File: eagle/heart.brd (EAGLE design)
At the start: 29.8 x 25.5 mm, 8 parts

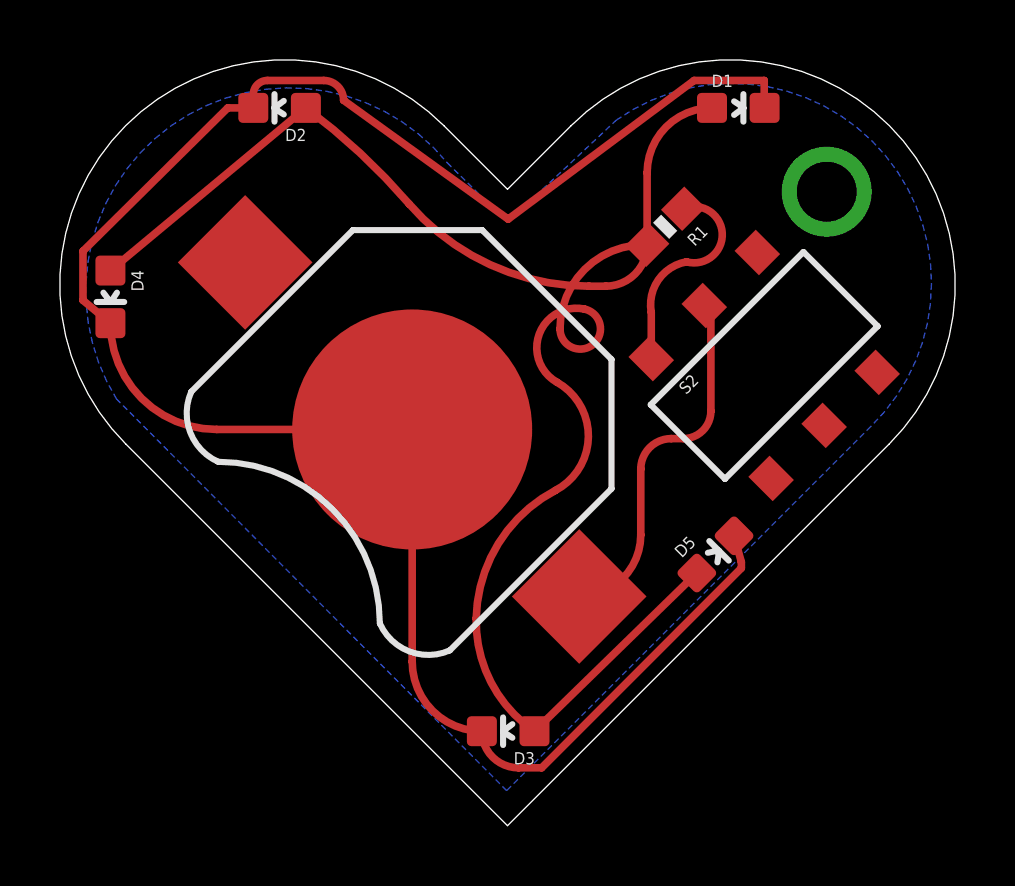
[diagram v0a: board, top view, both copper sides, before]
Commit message: move eagle files to `eagle` dir
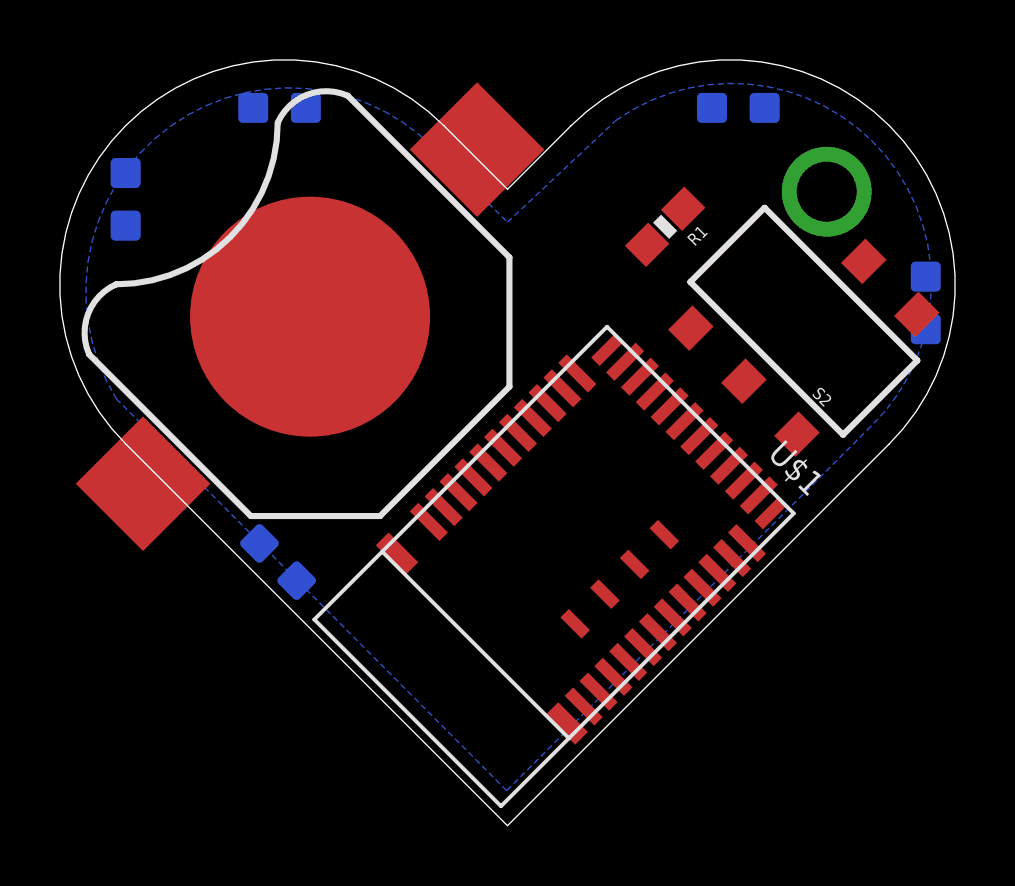
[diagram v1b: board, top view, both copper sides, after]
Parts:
- added U$1: MDBT42, MDBT42:MDBT42
- moved D3 19.9 mm to (30.7, 18.0), flipped to the bottom, turned to 0 degrees
- moved D5 14.6 mm to (9.14, 9.40), flipped to the bottom, turned to 135 degrees
- moved BAT1 5.07 mm to (10.2, 17.6), turned to 45 degrees
- moved D4 3.29 mm to (4.06, 21.5), flipped to the bottom, turned to 0 degrees
- moved S2 1.98 mm to (26.7, 17.4), turned to 135 degrees
- flipped D1 to the bottom
- flipped D2 to the bottom
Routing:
- net GND: track 67.7 -> 0.00 mm
- net VCC: track 55.9 -> 0.00 mm
- net N$2: track 11.8 -> 0.00 mm
- net N$4: track 5.37 -> 0.00 mm
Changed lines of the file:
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@@
 </autorouter>
 <elements>
-<element name="D1" library="SparkFun-LED" package="LED-0603" value="" x="24.4856" y="24.5364" rot="R270"/>
-<element name="D2" library="SparkFun-LED" package="LED-0603" value="" x="9.1948" y="24.5364" rot="R90"/>
-<element name="D3" library="SparkFun-LED" package="LED-0603" value="" x="16.8148" y="3.7592" rot="R90"/>
-<element name="D4" library="SparkFun-LED" package="LED-0603" value="" x="3.556" y="18.2372" rot="R180"/>
-<element name="BAT1" library="SparkFun-Electromechanical" package="BATTCON_12MM" value="" x="13.6144" y="13.8176" rot="R135">
-<attribute name="PROD_ID" value="BATT-08044" x="13.6144" y="13.8176" size="1.778" layer="27" rot="R135" display="off"/>
+<element name="D1" library="SparkFun-LED" package="LED-0603" value="" x="24.4856" y="24.5364" rot="MR270"/>
+<element name="D2" library="SparkFun-LED" package="LED-0603" value="" x="9.1948" y="24.5364" rot="MR90"/>
+<element name="D3" library="SparkFun-LED" package="LED-0603" value="" x="30.734" y="18.034" rot="MR0"/>
+<element name="D4" library="SparkFun-LED" package="LED-0603" value="" x="4.064" y="21.4884" rot="MR0"/>
+<element name="BAT1" library="SparkFun-Electromechanical" package="BATTCON_12MM" value="" x="10.2108" y="17.5768" rot="R45">
+<attribute name="PROD_ID" value="BATT-08044" x="10.2108" y="17.5768" size="1.778" layer="27" rot="R45" display="off"/>
 </element>
-<element name="S2" library="SparkFun-Electromechanical" package="AYZ0202_NOHOLE" value="" x="25.3492" y="15.9512" rot="R45"/>
+<element name="S2" library="SparkFun-Electromechanical" package="AYZ0202_NOHOLE" value="" x="26.67" y="17.4244" rot="R135"/>
 <element name="R1" library="SparkFun-Resistors" package="0603-RES" value="" x="22.0472" y="20.574" rot="R225"/>
-<element name="D5" library="SparkFun-LED" package="LED-0603" value="" x="23.7236" y="9.652" rot="R315"/>
+<element name="D5" library="SparkFun-LED" package="LED-0603" value="" x="9.144" y="9.398" rot="MR135"/>
+<element name="U$1" library="MDBT42" package="MDBT42" value="MDBT42" x="19.05" y="9.9568" rot="R135"/>
 </elements>
 <signals>
@@
 <contactref element="BAT1" pad="PWR@1"/>
 <contactref element="S2" pad="2"/>
-<wire x1="19.18215625" y1="8.249840625" x2="21.2344" y2="10.302084375" width="0.254" layer="1" curve="90"/>
-<wire x1="21.2344" y1="10.302084375" x2="21.2344" y2="12.4968" width="0.254" layer="1"/>
-<wire x1="21.2344" y1="12.4968" x2="22.2504" y2="13.5128" width="0.254" layer="1" curve="-90"/>
-<wire x1="22.2504" y1="13.5128" x2="22.6568" y2="13.5128" width="0.254" layer="1"/>
-<wire x1="22.6568" y1="13.5128" x2="23.5712" y2="14.4272" width="0.254" layer="1" curve="90"/>
-<wire x1="23.5712" y1="14.4272" x2="23.5712" y2="17.729196875" width="0.254" layer="1"/>
-<wire x1="23.5712" y1="17.729196875" x2="23.351621875" y2="17.948775" width="0.254" layer="1" curve="90"/>
+<wire x1="4.643040625" y1="12.009040625" x2="24.672421875" y2="15.426821875" width="0" layer="19" extent="1-1"/>
 </signal>
 <signal name="VCC">
@@
 <contactref element="D3" pad="A"/>
 <contactref element="D4" pad="A"/>
-<wire x1="10.0718" y1="24.5364" x2="3.556" y2="19.1142" width="0.254" layer="1"/>
 <contactref element="R1" pad="2"/>
-<wire x1="21.44615625" y1="19.97295625" x2="21.44615625" y2="22.37395625" width="0.254" layer="1"/>
-<wire x1="21.44615625" y1="22.37395625" x2="23.6086" y2="24.5364" width="0.254" layer="1" curve="-90"/>
-<wire x1="21.44615625" y1="19.97295625" x2="20.066" y2="18.5928" width="0.254" layer="1" curve="-90"/>
-<wire x1="20.066" y1="18.5928" x2="19.5072" y2="18.5928" width="0.254" layer="1"/>
-<wire x1="19.5072" y1="18.5928" x2="13.5128" y2="21.336" width="0.254" layer="1" curve="-49.180232"/>
-<wire x1="13.5128" y1="21.336" x2="10.0718" y2="24.5364" width="0.254" layer="1" curve="12.510026"/>
-<wire x1="21.44615625" y1="19.97295625" x2="21.34455625" y2="19.97295625" width="0.254" layer="1"/>
-<wire x1="21.34455625" y1="19.97295625" x2="18.542" y2="17.1704" width="0.254" layer="1" curve="90"/>
-<wire x1="18.542" y1="17.1704" x2="19.3548" y2="17.8308" width="0.254" layer="1" curve="258.187718"/>
-<wire x1="19.3548" y1="17.8308" x2="18.4404" y2="15.3924" width="0.254" layer="1" curve="162.511894"/>
-<wire x1="18.4404" y1="15.3924" x2="18.3896" y2="11.7856" width="0.254" layer="1" curve="-123.013685"/>
-<wire x1="18.3896" y1="11.7856" x2="15.748" y2="7.5184" width="0.254" layer="1" curve="61.108632"/>
-<wire x1="15.748" y1="7.5184" x2="17.6918" y2="3.7592" width="0.254" layer="1" curve="57.095303"/>
 <contactref element="D5" pad="A"/>
-<wire x1="23.103465625" y1="9.031865625" x2="17.6918" y2="3.7592" width="0.254" layer="1"/>
+<wire x1="21.44615625" y1="19.97295625" x2="25.3626" y2="24.5364" width="0" layer="19" extent="1-1"/>
+<wire x1="8.52386875" y1="10.01813125" x2="21.44615625" y2="19.97295625" width="0" layer="19" extent="1-1"/>
+<wire x1="30.734" y1="17.157" x2="8.52386875" y2="10.01813125" width="0" layer="19" extent="1-1"/>
+<wire x1="8.3178" y1="24.5364" x2="21.44615625" y2="19.97295625" width="0" layer="19" extent="1-1"/>
+<wire x1="4.064" y1="20.6114" x2="8.3178" y2="24.5364" width="0" layer="19" extent="1-1"/>
 </signal>
 <signal name="GND">
@@
 <contactref element="D2" pad="C"/>
 <contactref element="D1" pad="C"/>
-<wire x1="3.556" y1="17.3602" x2="7.0986" y2="13.8176" width="0.254" layer="1" curve="90"/>
-<wire x1="7.0986" y1="13.8176" x2="13.6144" y2="13.8176" width="0.254" layer="1"/>
-<wire x1="13.6144" y1="13.8176" x2="13.6144" y2="6.0826" width="0.254" layer="1"/>
-<wire x1="13.6144" y1="6.0826" x2="15.9378" y2="3.7592" width="0.254" layer="1" curve="90"/>
-<wire x1="3.556" y1="17.3602" x2="2.6416" y2="18.1222" width="0.254" layer="1"/>
-<wire x1="2.6416" y1="18.1222" x2="2.6416" y2="19.7612" width="0.254" layer="1"/>
-<wire x1="2.6416" y1="19.7612" x2="7.4676" y2="24.5364" width="0.254" layer="1"/>
-<wire x1="7.4676" y1="24.5364" x2="8.3178" y2="24.5364" width="0.254" layer="1"/>
-<wire x1="8.3178" y1="24.5364" x2="8.3178" y2="24.9802" width="0.254" layer="1"/>
-<wire x1="8.3178" y1="24.9802" x2="8.7884" y2="25.4508" width="0.254" layer="1" curve="-90"/>
-<wire x1="8.7884" y1="25.4508" x2="10.668" y2="25.4508" width="0.254" layer="1"/>
-<wire x1="10.668" y1="25.4508" x2="11.3284" y2="24.7904" width="0.254" layer="1" curve="-90"/>
-<wire x1="11.3284" y1="24.7904" x2="16.8148" y2="20.828" width="0.254" layer="1"/>
-<wire x1="16.8148" y1="20.828" x2="23.0124" y2="25.4508" width="0.254" layer="1"/>
-<wire x1="23.0124" y1="25.4508" x2="25.3492" y2="25.4508" width="0.254" layer="1"/>
-<wire x1="25.3492" y1="25.4508" x2="25.3492" y2="24.5498" width="0.254" layer="1"/>
-<wire x1="25.3492" y1="24.5498" x2="25.3626" y2="24.5364" width="0.254" layer="1" curve="90"/>
 <contactref element="D5" pad="C"/>
-<wire x1="24.34373125" y1="10.27213125" x2="24.5872" y2="9.398" width="0.254" layer="1"/>
-<wire x1="24.5872" y1="9.398" x2="24.5872" y2="9.1948" width="0.254" layer="1"/>
-<wire x1="24.5872" y1="9.1948" x2="17.9324" y2="2.54" width="0.254" layer="1"/>
-<wire x1="17.9324" y1="2.54" x2="17.157" y2="2.54" width="0.254" layer="1"/>
-<wire x1="17.157" y1="2.54" x2="15.9378" y2="3.7592" width="0.254" layer="1" curve="-90"/>
+<wire x1="9.764134375" y1="8.777865625" x2="23.6086" y2="24.5364" width="0" layer="19" extent="1-1"/>
+<wire x1="30.734" y1="18.911" x2="9.764134375" y2="8.777865625" width="0" layer="19" extent="1-1"/>
+<wire x1="10.2108" y1="17.5768" x2="30.734" y2="18.911" width="0" layer="19" extent="1-1"/>
+<wire x1="10.0718" y1="24.5364" x2="10.2108" y2="17.5768" width="0" layer="19" extent="1-1"/>
+<wire x1="4.064" y1="22.3654" x2="10.0718" y2="24.5364" width="0" layer="19" extent="1-1"/>
 </signal>
 <signal name="N$3">
@@
 <contactref element="S2" pad="1"/>
 <contactref element="R1" pad="1"/>
-<wire x1="21.58385625" y1="16.181009375" x2="21.58385625" y2="17.72305625" width="0.254" layer="1"/>
-<wire x1="21.58385625" y1="17.72305625" x2="22.7584" y2="19.4056" width="0.254" layer="1" curve="-90"/>
-<wire x1="22.7584" y1="19.4056" x2="22.648240625" y2="21.175040625" width="0.254" layer="1" curve="218.51398"/>
+<wire x1="26.4401875" y1="13.65905625" x2="22.648240625" y2="21.175040625" width="0" layer="19" extent="1-1"/>
 </signal>
 </signals>
